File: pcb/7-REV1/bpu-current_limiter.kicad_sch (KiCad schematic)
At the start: 44 parts, among them Q401 BCM857, Q402 BC2301T 2.8A, Q601 MMDT3906, Q602 BC2301T 2.8A, U4 MCP4725xxx-xCH, U5 MCP4725xxx-xCH, U601 GS321A-TR, U602 GSV331-TR

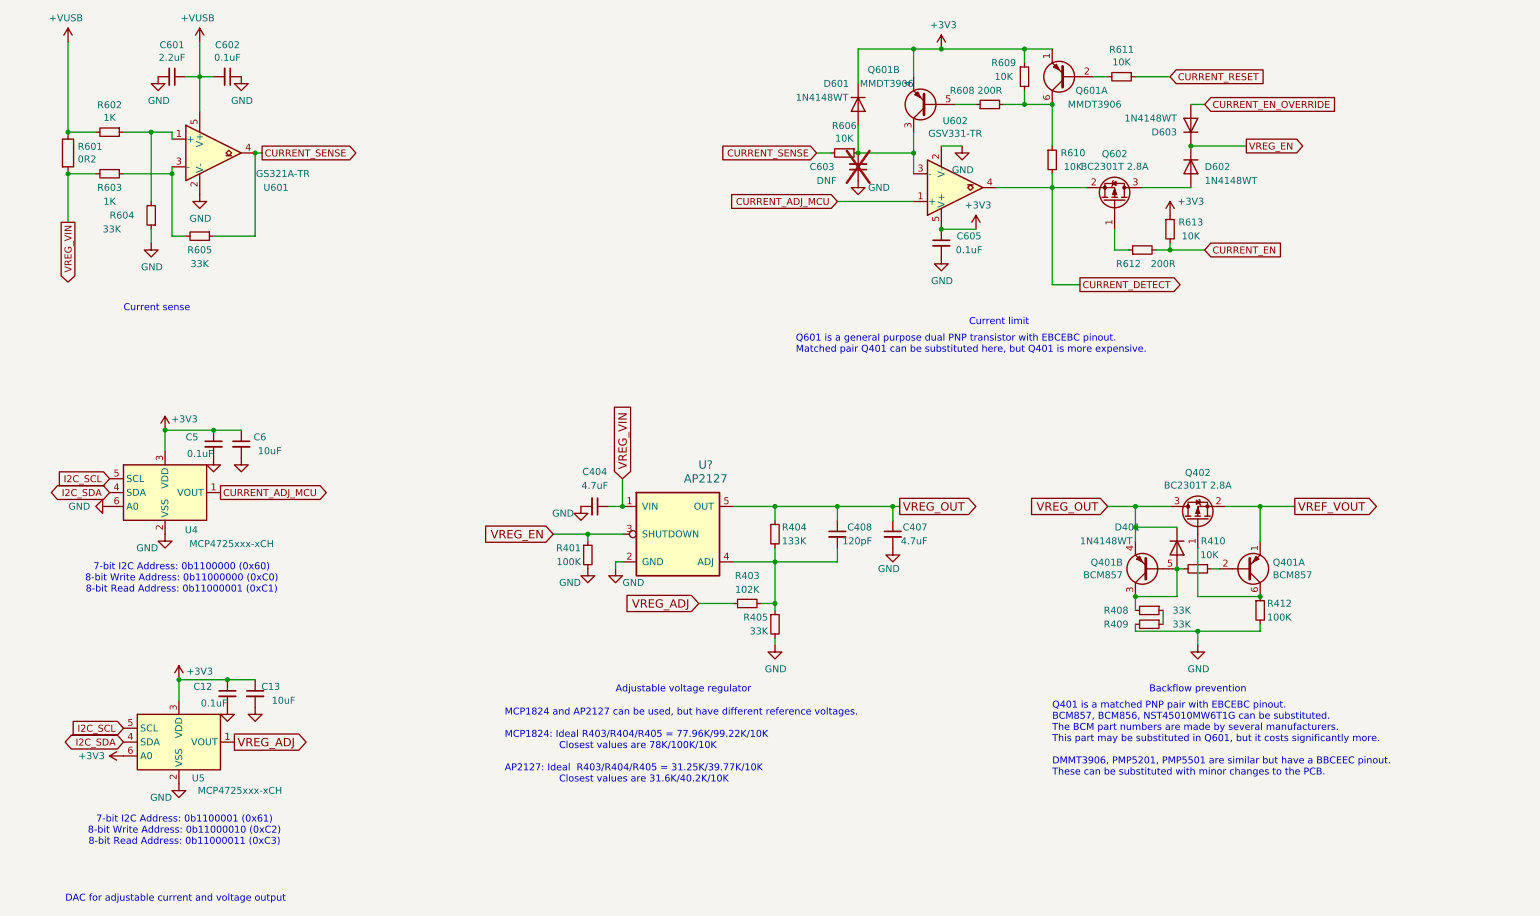
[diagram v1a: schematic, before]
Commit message: adapt protection for the AP2127 voltage regulator
- add a PMEG2020EJ for backflow-handling
- remove the previous backflow protection circuit
- remove the AP2127+circuit from the "VOUT protection" sheet, it was redundant
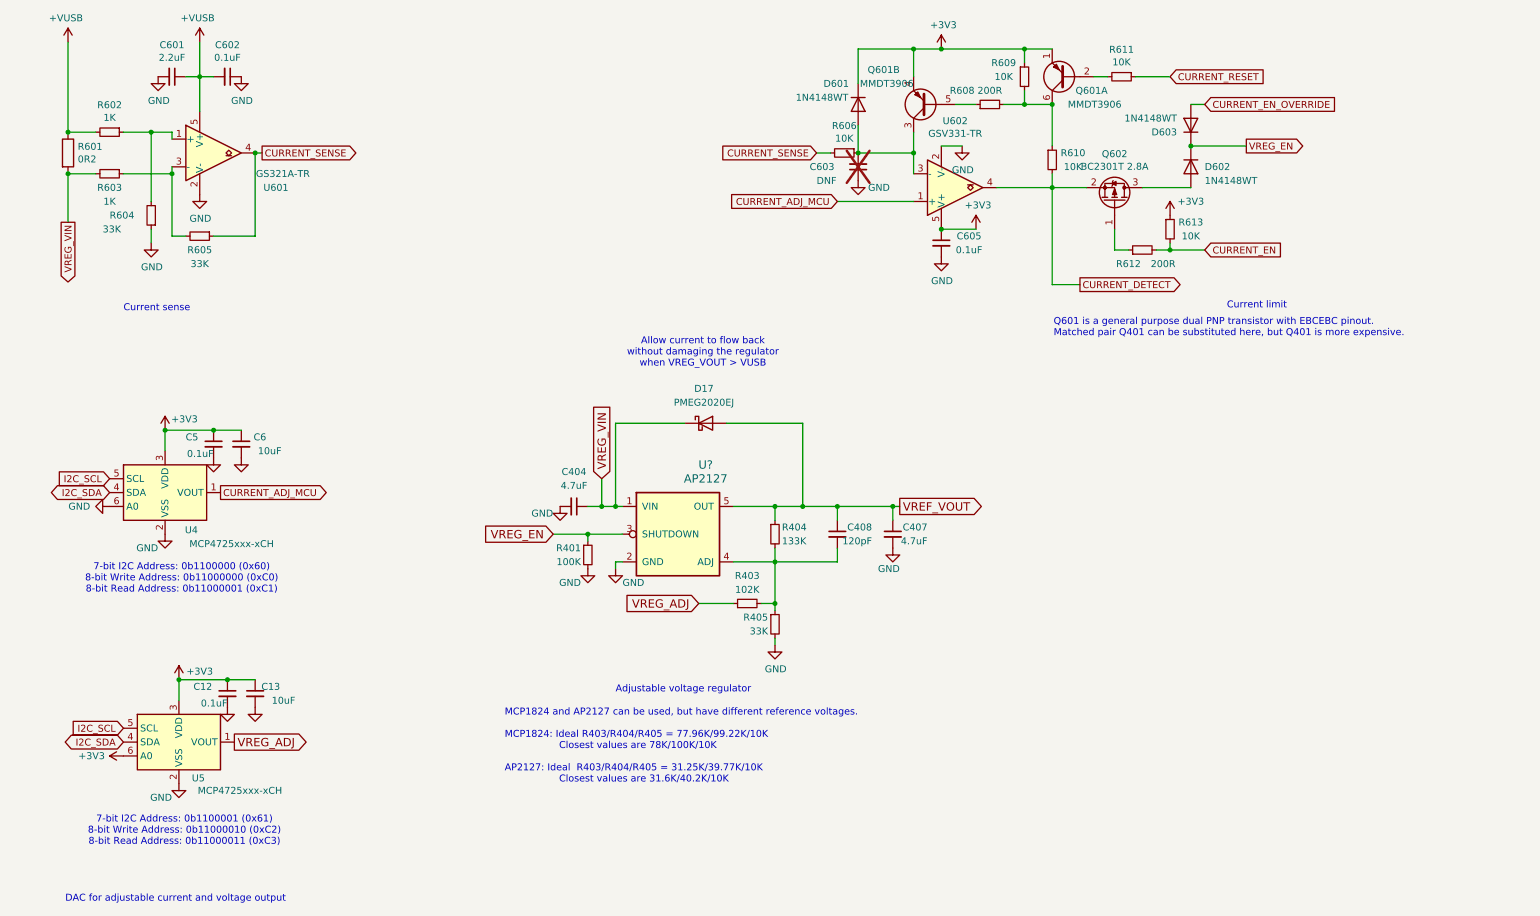
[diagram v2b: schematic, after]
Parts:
- removed D401: 1N4148WT, Diode_SMD:D_SOD-523, symbol Diode:1N4148WS
- removed Q401: BCM857, Package_TO_SOT_SMD:SOT-363_SC-70-6, symbol kicad5-device:Q_DUAL_PNP_PNP_E1B1C2E2B2C1
- removed Q402: BC2301T 2.8A, Package_TO_SOT_SMD:SOT-523, symbol Transistor_FET:BSS84
- removed R408, R409: 33K, Resistor_SMD:R_0402_1005Metric, symbol Device:R_Small
- removed R410: 10K, Resistor_SMD:R_0402_1005Metric, symbol Device:R_Small
- removed R412: 100K, Resistor_SMD:R_0402_1005Metric, symbol Device:R_Small
- added D17: PMEG2020EJ, Diode_SMD:D_SOD-323F, symbol Device:D_Schottky
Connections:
- net VREG_OUT is gone; now on net VREF_VOUT: C407.1, C408.1, R404.1, U?.5 (OUT)
- net VREF_VOUT: now also D17.2 (A)
- net VREG_VIN: now also D17.1 (K)
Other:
- note added: "Allow current to flow back without damaging the regulator when VREG_VOUT > VUSB"
- note removed: "Backflow prevention"
- note removed: "Q401 is a matched PNP pair with EBCEBC pinout. BCM857, BCM856, NST45010MW6T1G can be substituted. The BCM part numbers are made by several manufacturers. This part may be substituted in Q601, but it costs significantly more. DMMT3906, PMP5201, PMP5501 are similar but have a BBCEEC pinout. These can be substituted with minor changes to the PCB."
- moved on the sheet: C404

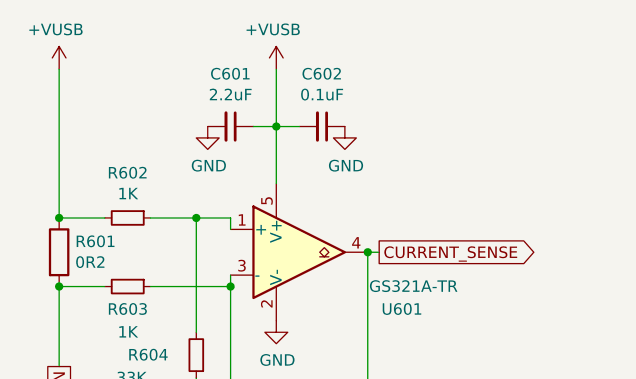
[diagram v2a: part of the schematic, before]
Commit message: TCA6416ARTWR IO expander, 2.2uF->4.7uF
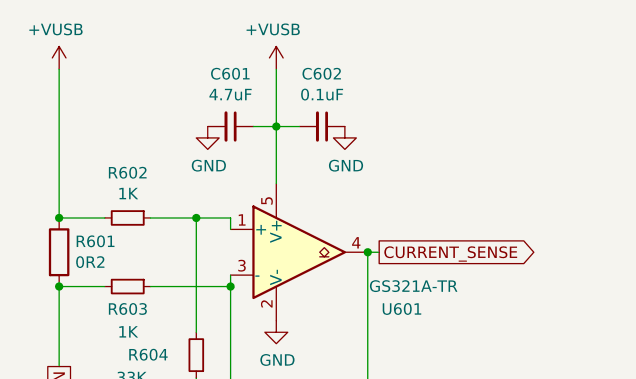
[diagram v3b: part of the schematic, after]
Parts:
- C601: value 2.2uF -> 4.7uF
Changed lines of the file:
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@@
 			)
 		)
-		(property "Value" "2.2uF"
+		(property "Value" "4.7uF"
 			(at 40.64 24.4348 90)
 			(effects

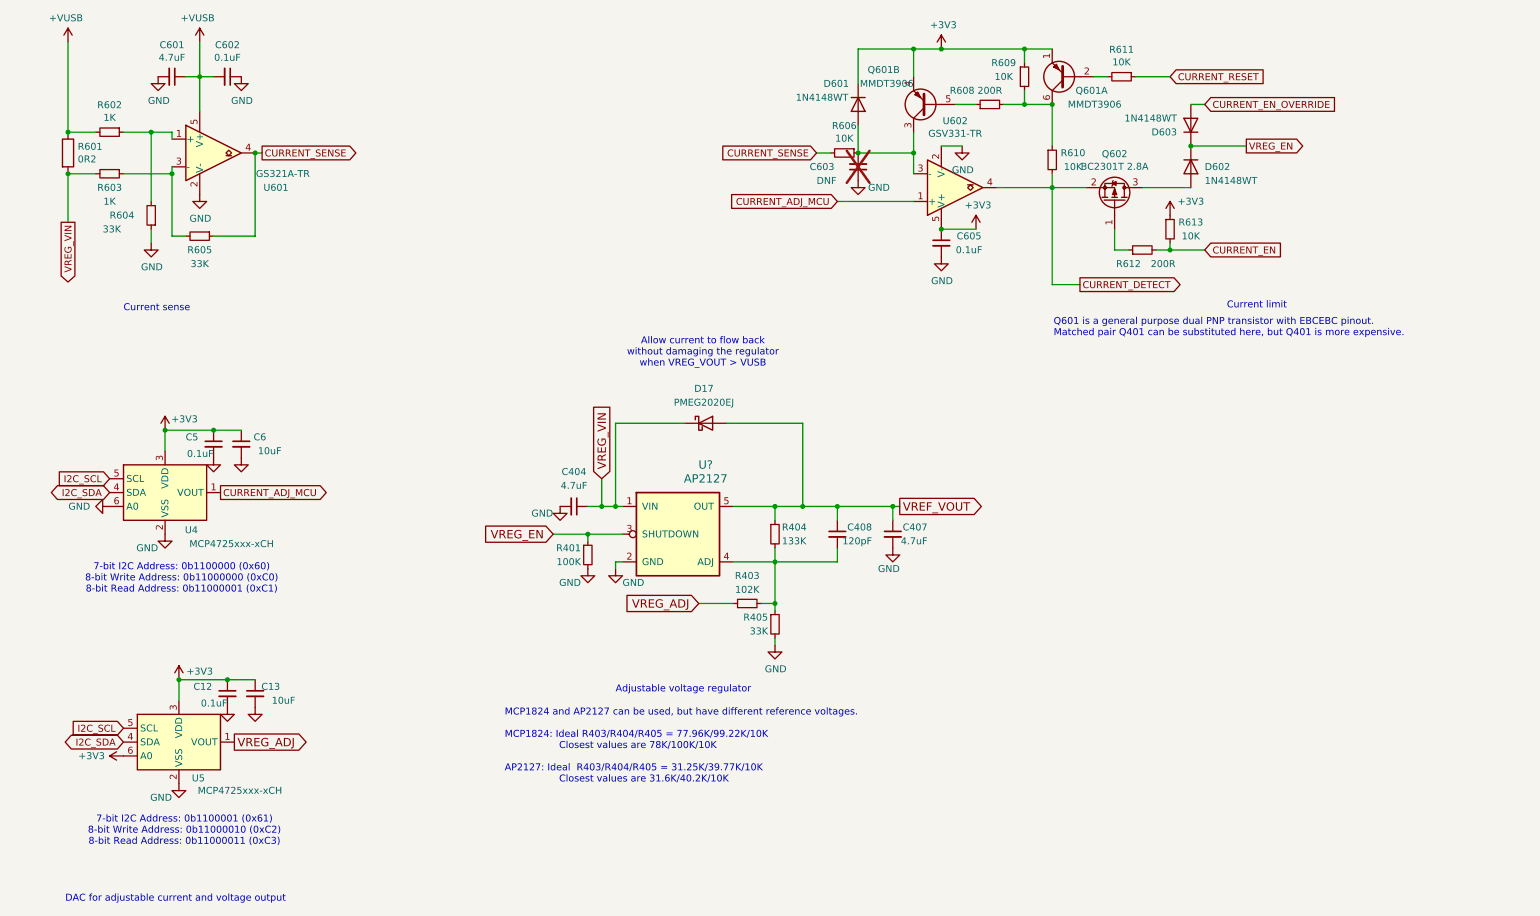
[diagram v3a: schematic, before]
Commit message: BP7REV1 2.2uF, 4.7uF-> 10uF/6.3V CL05A106MQ5NUN. 520K->470K on reset/bootloader switch.
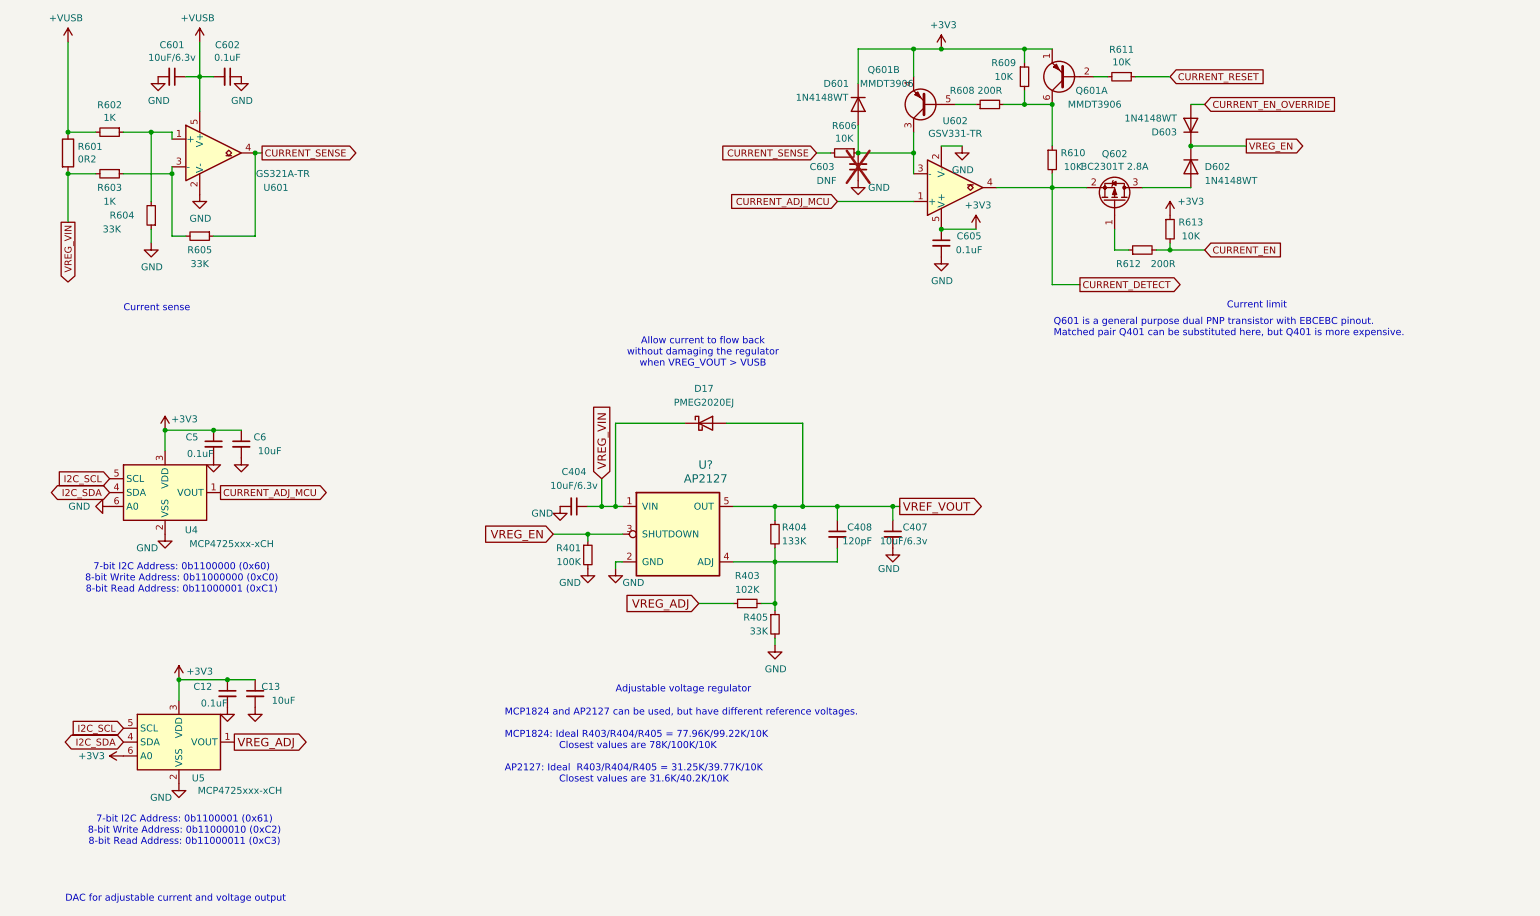
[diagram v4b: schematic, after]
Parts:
- C404, C407, C601: value 4.7uF -> 10uF/6.3v
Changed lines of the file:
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@@
 			)
 		)
-		(property "Value" "4.7uF"
+		(property "Value" "10uF/6.3v"
 			(at 179.07 113.03 0)
 			(effects
@@
 			)
 		)
-		(property "Description" ""
+		(property "Description" "CL05A106MQ5NUN"
 			(at 172.72 111.76 0)
 			(effects
@@
 			)
 		)
-		(property "Value" "4.7uF"
+		(property "Value" "10uF/6.3v"
 			(at 114.3 102.87 90)
 			(effects
@@
 			)
 		)
-		(property "Description" ""
+		(property "Description" "CL05A106MQ5NUN"
 			(at 114.3 106.68 0)
 			(effects
@@
 			)
 		)
-		(property "Value" "4.7uF"
+		(property "Value" "10uF/6.3v"
 			(at 40.64 24.4348 90)
 			(effects
@@
 			)
 		)
-		(property "Description" ""
+		(property "Description" "CL05A106MQ5NUN"
 			(at 40.64 27.94 0)
 			(effects

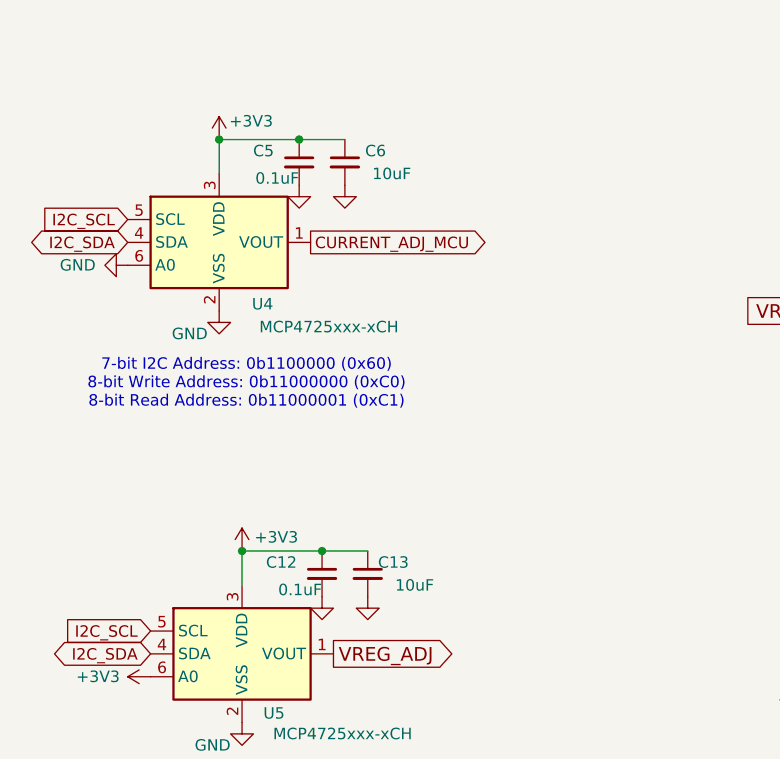
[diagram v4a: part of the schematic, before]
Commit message: specify part numbers and manufacturers in more detail - 10µF / 0805 caps - 2N7002KT fets
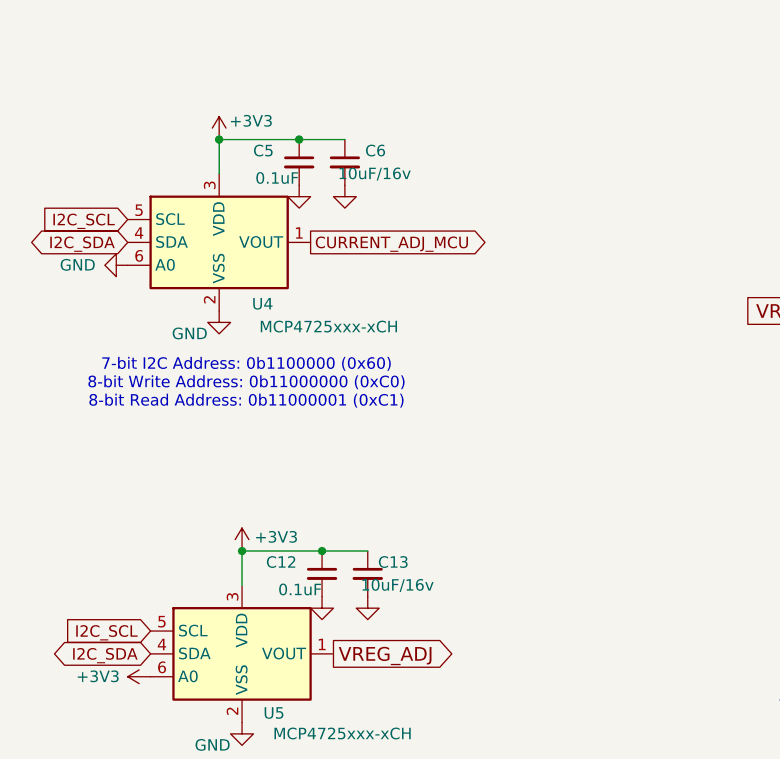
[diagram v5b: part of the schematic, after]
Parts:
- C13, C6: value 10uF -> 10uF/16v; MANUFACTURER (none) -> Samsung
- C404, C407, C601: MANUFACTURER (none) -> Samsung
- D17: MANUFACTURER (none) -> Nexperia

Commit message: reorg, but forgot to check changes first :(
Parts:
- removed C12, C5: 0.1uF, Capacitor_SMD:C_0402_1005Metric, symbol Device:C_Small
- removed C13, C6: 10uF/16v, Capacitor_SMD:C_0805_2012Metric, symbol Device:C_Small
- removed U4, U5: MCP4725xxx-xCH, Package_TO_SOT_SMD:SOT-23-6, symbol Analog_DAC:MCP4725xxx-xCH
- added C413: 2.2uF, Capacitor_SMD:C_0402_1005Metric, symbol Device:C_Small
- added C414, C415, C416: 0.1uF, Capacitor_SMD:C_0402_1005Metric, symbol Device:C_Small
- added D10: SMF5.0A, Diode_SMD:D_SMF, symbol Diode:SMAJ5.0A
- added D401: 1N4148WT, Diode_SMD:D_SOD-523, symbol Diode:1N4148WS
- added Q401: BCM857, Package_TO_SOT_SMD:SOT-363_SC-70-6, symbol kicad5-device:Q_DUAL_PNP_PNP_E1B1C2E2B2C1
- added Q402: BC2301T 2.8A, Package_TO_SOT_SMD:SOT-523, symbol Transistor_FET:BSS84
- added R408, R409: 33K, Resistor_SMD:R_0402_1005Metric, symbol Device:R_Small
- added R410, R414, R415: 10K, Resistor_SMD:R_0402_1005Metric, symbol Device:R_Small
- added R412: 100K, Resistor_SMD:R_0402_1005Metric, symbol Device:R_Small
- added U603: LMV321, Package_TO_SOT_SMD:SOT-23-5, symbol Comparator:LMV331
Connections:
- net +3V3: now also C413.1, C414.2, U603.5 (V+)
- net CURRENT_ADJ_MCU: now also R415.2; no longer U602.1 (+)
- net GND: now also C413.2, C414.1, C415.1, C416.1, D10.2 (A2), R409.2, R412.2, U603.2 (V-)
- net VREF_VOUT: now also D10.1 (A1), Q401.1 (E1), Q402.2 (S); no longer C407.1, C408.1, D17.2 (A), R404.1, U?.5 (OUT)
- net VREG_ADJ: now also U603.3 (-), U603.4
- new net: C416.2, R415.1, U602.1 (+)
- new net: C415.2, R414.1, U603.1 (+)
- new net: D401.2 (A), Q401.3 (C2), Q401.5 (B2), R408.2, R410.2
- new net: Q401.2 (B1), R410.1
- new net: R408.1, R409.1
- new net: Q401.6 (C1), Q402.1 (G), R412.1
- new net VREG_ADJ_MCU: R414.2
- new net VREG_OUT: C407.1, C408.1, D17.2 (A), D401.1 (K), Q401.4 (E2), Q402.3 (D), R404.1, U?.5 (OUT)
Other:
- note added: "Backflow prevention"
- note added: "Buffer circuit for Voltage Adjust, when using the MCU to do PWM instead U406 as DAC"
- note added: "Q401 is a matched PNP pair with EBCEBC pinout. BCM857, BCM856, NST45010MW6T1G can be substituted. The BCM part numbers are made by several manufacturers. This part may be substituted in Q601, but it costs significantly more. DMMT3906, PMP5201, PMP5501 are similar but have a BBCEEC pinout. These can be substituted with minor changes to the PCB."
- note removed: "7-bit I2C Address: 0b1100000 (0x60) 8-bit Write Address: 0b11000000 (0xC0) 8-bit Read Address: 0b11000001 (0xC1)"
- note removed: "7-bit I2C Address: 0b1100001 (0x61) 8-bit Write Address: 0b11000010 (0xC2) 8-bit Read Address: 0b11000011 (0xC3)"
- note removed: "DAC for adjustable current and voltage output"
